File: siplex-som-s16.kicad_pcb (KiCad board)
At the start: 8 copper layers, 30 x 30 mm, 58 parts, among them J1 RFShield_OnePiece, J2 Conn_01x20, J3 Conn_01x20, J4 Conn_01x20, J6 Conn_01x20, U1 STM32H743IIKx, U2 IS42S16160J-6BLI, U3 W25Q32JVZP, U4 AP2112K-3.3, U5 W25Q32JVZP, Y1 25MHz, Y2 32.768KHz

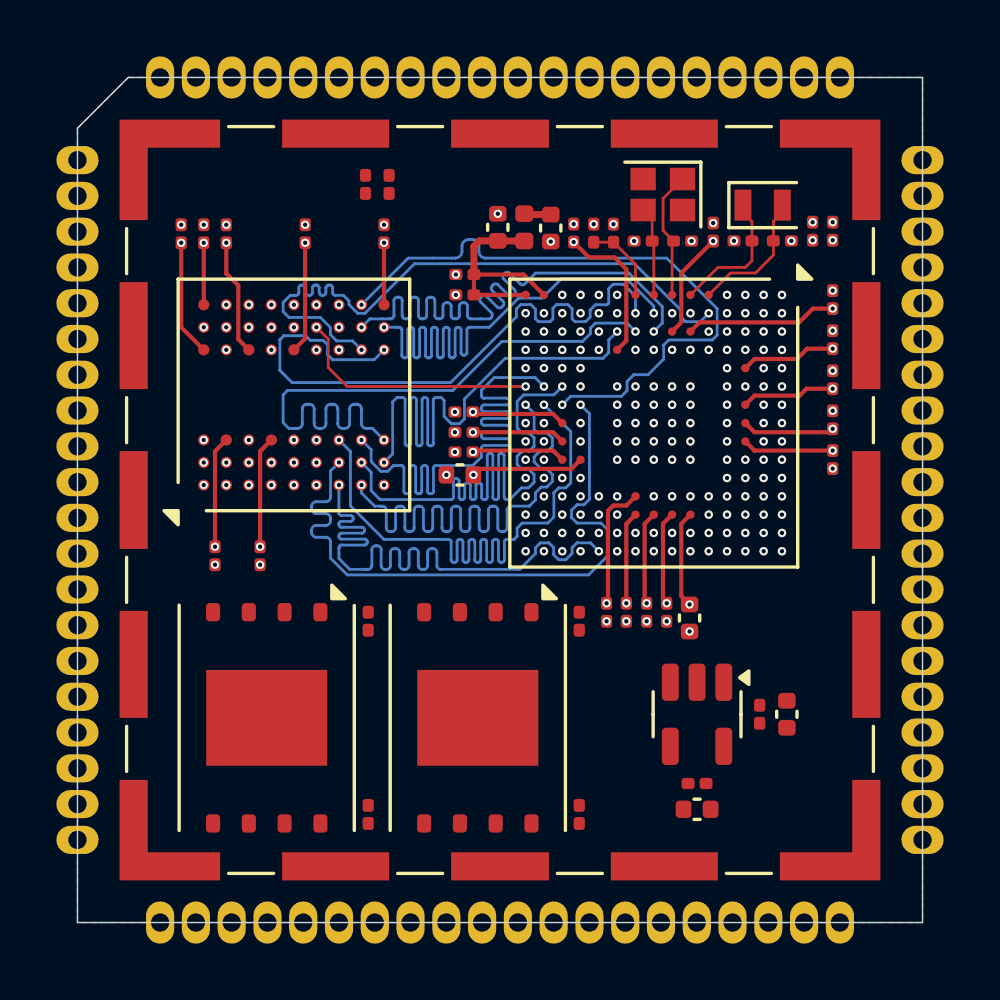
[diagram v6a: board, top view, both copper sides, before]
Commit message: Modify SDRAM tracks as its conflicted with FLASH tracks
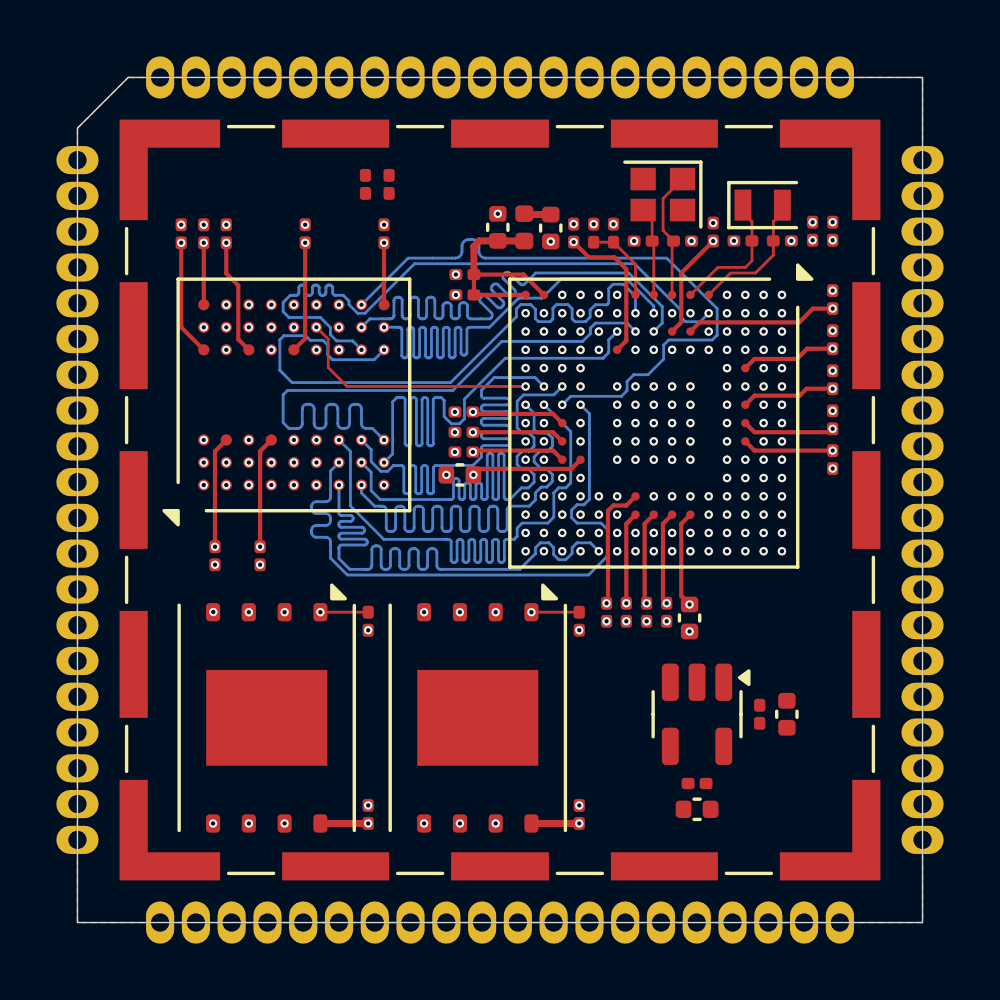
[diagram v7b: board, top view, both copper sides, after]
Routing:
- net /MCU/FLASH_BK1_IO0: track 0.00 -> 28.2 mm, vias 1 -> 2
- net /MCU/~{FLASH_BK1_CS}: track 0.00 -> 26.6 mm, vias 1 -> 2
- net /MCU/FLASH_BK1_IO3: track 0.00 -> 25.0 mm, vias 1 -> 2
- net /MCU/FLASH_BK2_IO3: track 0.00 -> 24.8 mm, vias 1 -> 2
- net /MCU/FLASH_BK2_IO0: track 0.00 -> 22.1 mm, vias 1 -> 2
- net /MCU/FLASH_BK1_IO2: track 0.00 -> 19.3 mm, vias 1 -> 2
- net /MCU/FLASH_BK1_IO1: track 0.00 -> 18.0 mm, vias 1 -> 2
- net /MCU/FLASH_BK2_IO1: track 0.00 -> 14.1 mm, vias 1 -> 2
- net /MCU/~{FLASH_BK2_CS}: track 0.00 -> 11.7 mm, vias 1 -> 2
- net /MCU/FLASH_CLK: track 0.00 -> 8.06 mm, vias 1 -> 3
- net /MCU/SDRAM_DQMH: track 44.1 -> 36.1 mm
- net +3V3: track 77.6 -> 81.0 mm, vias 23 -> 27
- net /MCU/SDRAM_DQML: track 21.2 -> 20.5 mm
- net /MCU/SDRAM_DQ15: track 25.4 -> 25.9 mm
- net GND: track 0.00 -> 0.01 mm, vias 79 -> 83
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
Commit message: Finished FLASH tracks
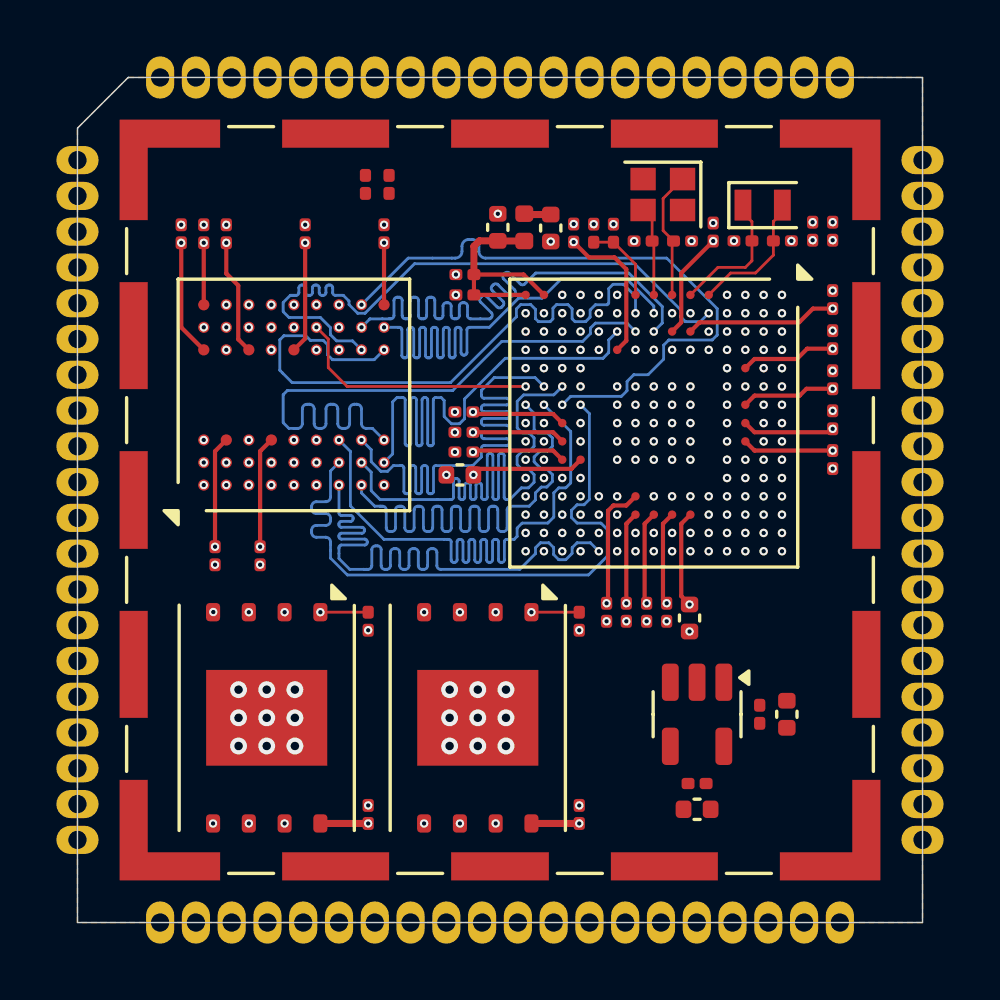
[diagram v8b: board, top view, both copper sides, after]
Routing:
- net /MCU/FLASH_BK2_IO2: track 0.00 -> 33.7 mm
- net /MCU/FLASH_CLK: track 8.06 -> 33.8 mm
- net /MCU/~{FLASH_BK2_CS}: track 11.7 -> 35.5 mm
- net /MCU/FLASH_BK2_IO1: track 14.1 -> 33.8 mm
- net /MCU/FLASH_BK1_IO1: track 18.0 -> 33.8 mm
- net /MCU/FLASH_BK1_IO2: track 19.3 -> 33.7 mm
- net /MCU/FLASH_BK2_IO0: track 22.1 -> 33.8 mm
- net /MCU/FLASH_BK2_IO3: track 24.8 -> 33.7 mm
- net /MCU/FLASH_BK1_IO3: track 25.0 -> 33.7 mm
- net /MCU/~{FLASH_BK1_CS}: track 26.6 -> 33.8 mm
- net /MCU/FLASH_BK1_IO0: track 28.2 -> 33.7 mm
- net GND: track 0.01 -> 0.17 mm, vias 83 -> 101
